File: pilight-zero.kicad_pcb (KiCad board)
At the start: 2 copper layers, 65 x 30 mm, 10 parts, among them J1 GPIO partial, U1 RX-4M50RR30SF, U2 TX_433Mhz

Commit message: Replaced R2 by pot
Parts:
- R2: value 820k -> 1M; footprint Resistor_THT:R_Axial_DIN0207_L6.3mm_D2.5mm_P7.62mm_Horizontal -> Potentiometer_THT:Potentiometer_ACP_CA9-H2,5_Horizontal
- moved R2 11.9 mm to (122.7, 107.9), turned to 180 degrees
- moved U2 0.76 mm to (170.1, 107.3)
- moved AE1 0.52 mm to (157.1, 99.5)
- moved U1 0.51 mm to (159.6, 103.5)
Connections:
- J1 pad 10: /GPIO15_RXD0 -> (no net)
- J1 pad 13: /GPIO27_GEN2 -> (no net)
- J1 pad 15: /GPIO22_GEN3 -> (no net)
- J1 pad 16: /GPIO23_GEN4 -> (no net)
- J1 pad 18: /GPIO24_GEN5 -> (no net)
- J1 pad 19: /GPIO10_SPI_MOSI -> (no net)
- J1 pad 21: /GPIO9_SPI_MISO -> (no net)
- J1 pad 22: /GPIO25_GEN6 -> (no net)
- J1 pad 23: /GPIO11_SPI_SCLK -> (no net)
- J1 pad 24: /GPIO8_SPI_CE0_N -> (no net)
- J1 pad 26: /GPIO7_SPI_CE1_N -> (no net)
- J1 pad 3: /GPIO2_SDA1 -> (no net)
- J1 pad 5: /GPIO3_SCL1 -> (no net)
- J1 pad 7: /GPIO4_GPIO_GCLK -> (no net)
- J1 pad 8: /GPIO14_TXD0 -> (no net)
- R2 pad 2: GND -> Net-(R2-Pad2)
- U1 pad 13: Net-(R2-Pad1) -> Net-(R2-Pad2)
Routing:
- net GND: track 72.8 -> 0.00 mm
- net Net-(R2-Pad2): track 0.00 -> 12.3 mm
- net Net-(R2-Pad1): track 3.81 -> 0.00 mm
- net Net-(J1-Pad11): track 33.3 -> 34.1 mm
- net +5V: track 58.4 -> 59.0 mm
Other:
- board text added: "pilight-zero v1.2"
- board text removed: "pilight-zero v1.0"

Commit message: Add 3D model for trimmer
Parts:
- R2: footprint Potentiometer_THT:Potentiometer_ACP_CA9-H2,5_Horizontal -> lib:Potentiometer_ACP_CA9-H2,5_Horizontal
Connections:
- R2 pad 1: Net-(R2-Pad1) -> (no net)

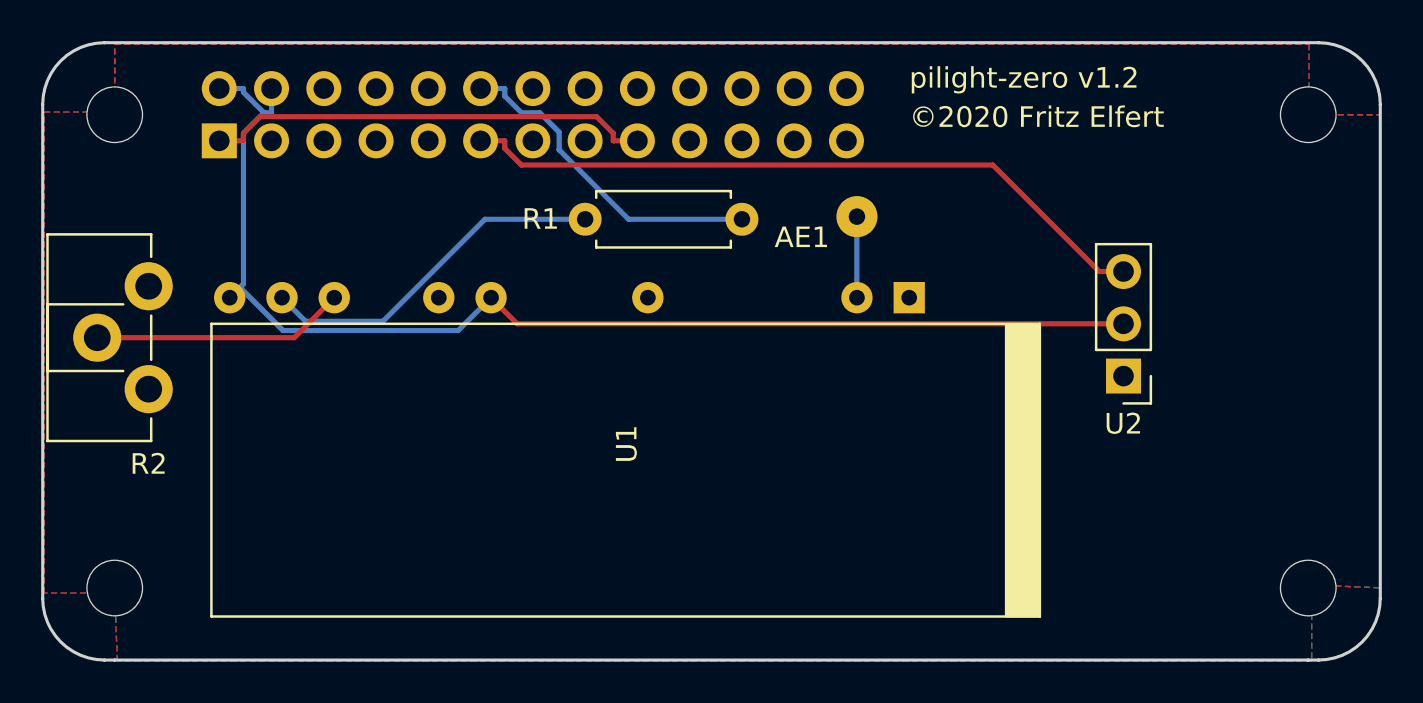
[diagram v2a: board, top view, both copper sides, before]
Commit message: Misc fixes and additions
 - Fixed pad dimensions of potentiometer
 - Added pinheader and resistors for
   - Power button
   - Power LED
   - Wifi LED
   - 433Mhz TX LED
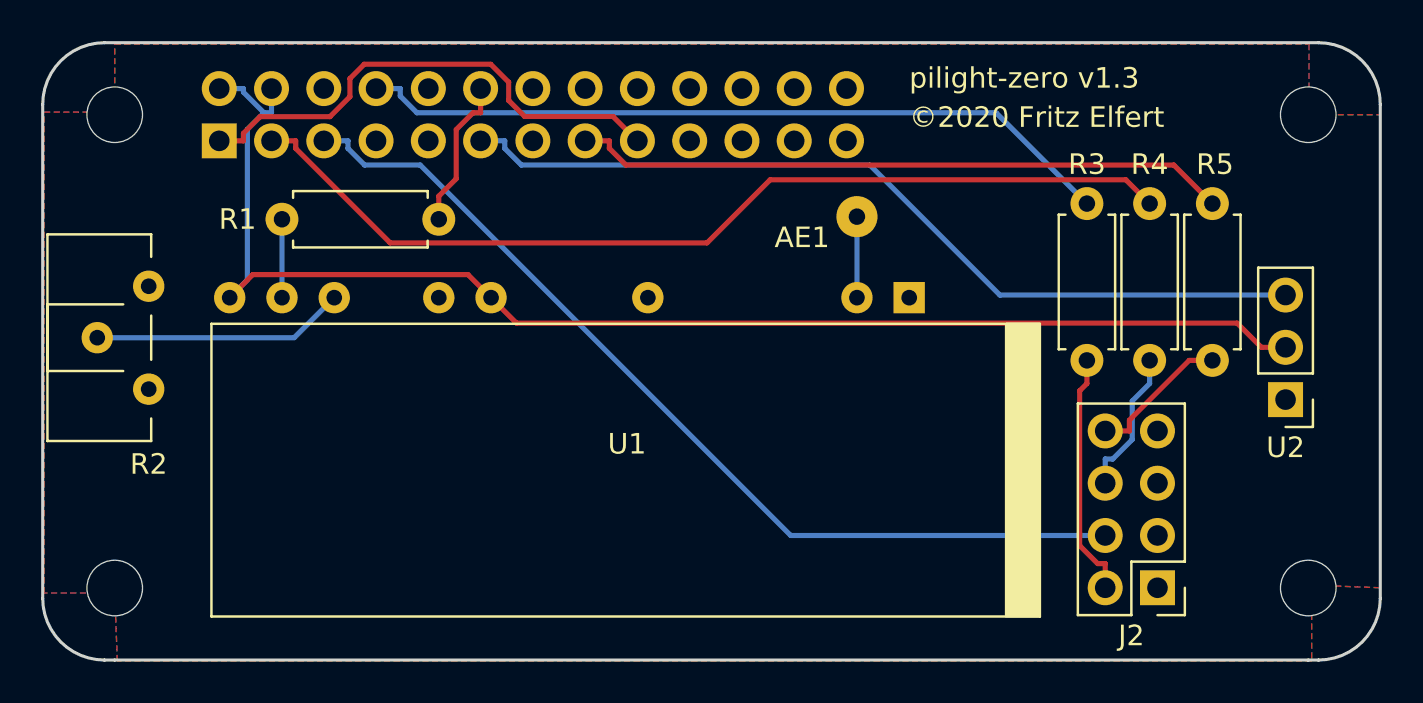
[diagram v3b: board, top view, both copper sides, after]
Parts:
- added J2: Conn_02x04_Odd_Even, Connector_PinHeader_2.54mm:PinHeader_2x04_P2.54mm_Vertical, F.Cu at (171.7, 117.6)
- added R3: 1k, Resistor_THT:R_Axial_DIN0207_L6.3mm_D2.5mm_P7.62mm_Horizontal, F.Cu at (168.3, 98.9)
- added R4: 1k, Resistor_THT:R_Axial_DIN0207_L6.3mm_D2.5mm_P7.62mm_Horizontal, F.Cu at (171.3, 98.9)
- added R5: 1k, Resistor_THT:R_Axial_DIN0207_L6.3mm_D2.5mm_P7.62mm_Horizontal, F.Cu at (174.4, 98.9)
- moved R1 14.7 mm to (129.2, 99.6)
- moved U2 7.96 mm to (177.9, 108.4)
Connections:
- net Net-(J1-Pad11) renamed /GPIO17_GEN0
- J1 pad 15: (no net) -> /GPIO22_GEN3
- J1 pad 3: (no net) -> /GPIO2_SDA1
- J1 pad 5: (no net) -> /GPIO3_SCL1
- J1 pad 8: (no net) -> /GPIO14_TXD0
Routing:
- net /GPIO2_SDA1: track 0.00 -> 46.7 mm
- net /GPIO3_SCL1: track 0.00 -> 46.1 mm
- net /GPIO14_TXD0: track 0.00 -> 37.1 mm
- net /GPIO22_GEN3: track 0.00 -> 32.0 mm
- net Net-(R1-Pad1): track 17.3 -> 3.81 mm
- net /PwrLED: track 0.00 -> 11.9 mm
- net /GPIO18_GEN1: track 16.1 -> 7.41 mm
- net /GPIO17_GEN0: track 34.1 -> 42.4 mm
- net +5V: track 59.0 -> 67.2 mm
- net /WifiLED: track 0.00 -> 7.08 mm
- net /TxLED: track 0.00 -> 6.93 mm
- net +3V3: track 21.7 -> 24.7 mm
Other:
- board text added: "pilight-zero v1.3"
- board text removed: "pilight-zero v1.2"

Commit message: Updated misc 3d models
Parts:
- U2: footprint Connector_PinHeader_2.54mm:PinHeader_1x03_P2.54mm_Vertical -> lib:TX-433Mhz

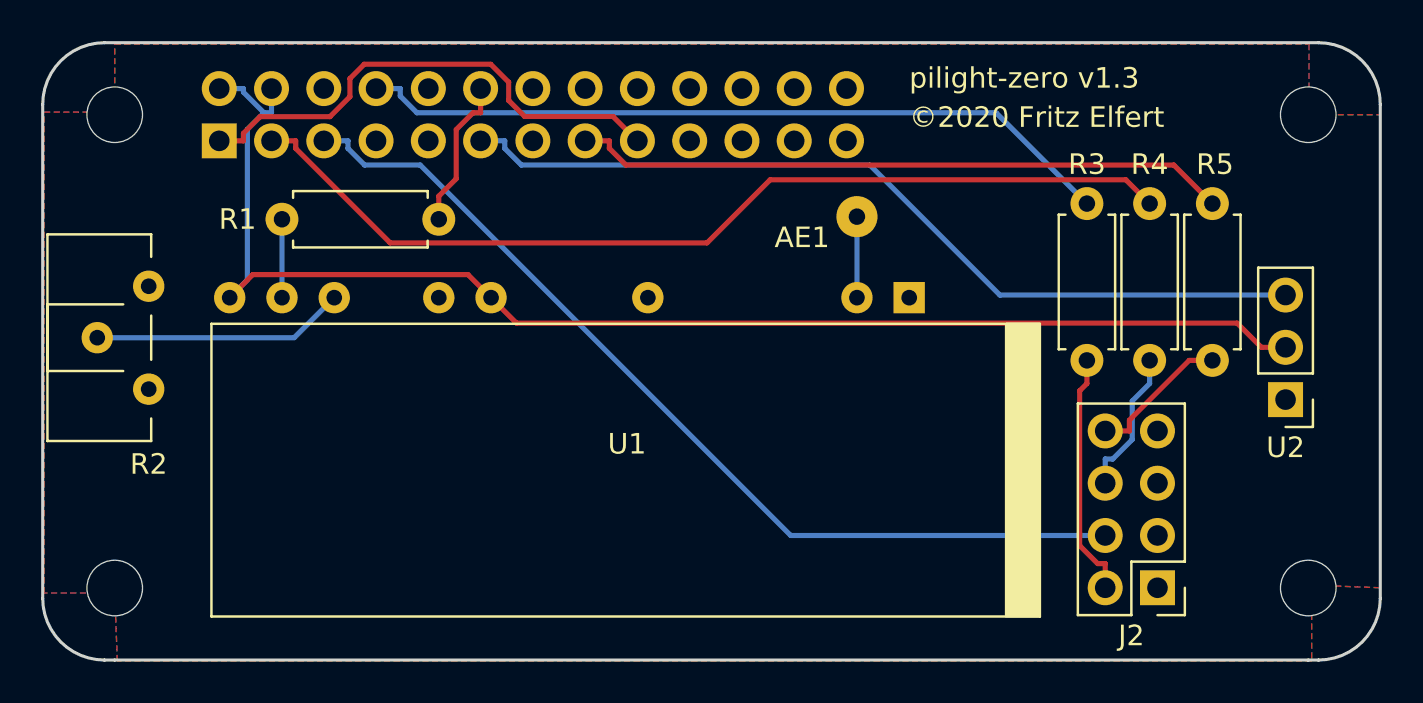
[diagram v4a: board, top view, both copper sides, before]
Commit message: Changed WifiLED output to GPIO27
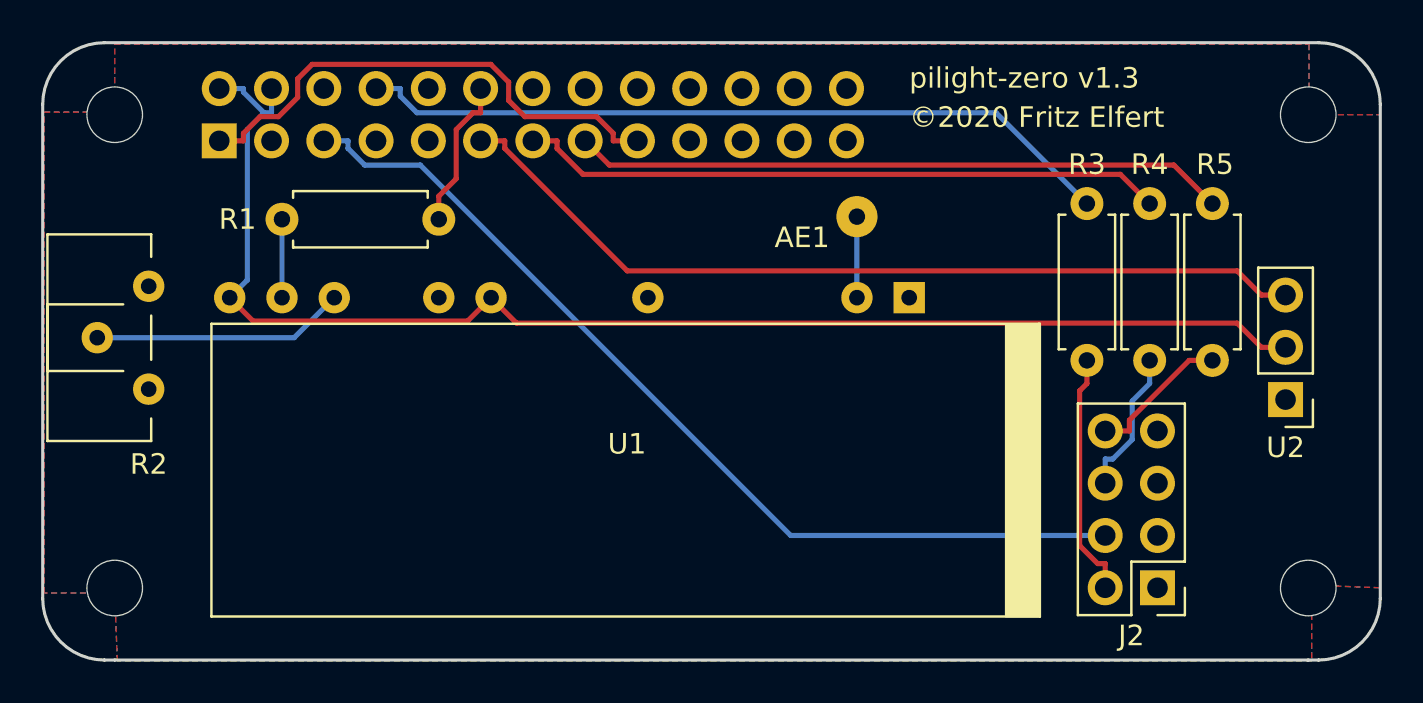
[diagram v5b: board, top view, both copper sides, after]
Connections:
- J1 pad 13: (no net) -> /GPIO27_GEN2
- J1 pad 3: /GPIO2_SDA1 -> (no net)
- R4 pad 1: /GPIO2_SDA1 -> /GPIO27_GEN2
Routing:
- net /GPIO2_SDA1: track 46.7 -> 0.00 mm
- net /GPIO27_GEN2: track 0.00 -> 31.4 mm

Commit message: Bumped silk version number
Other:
- board text added: "pilight-zero v1.4"
- board text removed: "pilight-zero v1.3"
